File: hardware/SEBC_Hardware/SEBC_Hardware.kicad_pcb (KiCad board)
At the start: 2 copper layers, 38 parts, among them J1 Barrel_Jack_Switch, J2 Conn_01x01_Female, J3 Conn_01x01_Female, J4 AudioJack2_Ground_Switch, J5 Conn_01x01_Female, J6 Conn_01x01_Female, J7 AudioJack2_Ground_Switch, J8 Micro_SD_Card, SW1 SW_Push, SW2 SW_Push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

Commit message: :construction: SEBC PCB
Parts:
- moved C7 210.7 mm to (53.3, 53.3)
- moved C2 208.3 mm to (61.5, 59.9)
- moved R8 202.2 mm to (63.5, 40.6), turned to 270 degrees
- moved D4 195.3 mm to (76.7, 81.3)
- moved C1 191.8 mm to (61.5, 53.3)
- moved C4 186.1 mm to (77.7, 37.1)
- moved SW2 173.8 mm to (91.7, 29.3), turned to 90 degrees
- moved R3 158.6 mm to (86.9, 36.6), turned to 90 degrees
- moved SW1 150.2 mm to (96.8, 36.3), turned to 270 degrees
- moved R4 129.2 mm to (107.3, 36.8), turned to 90 degrees
- moved D3 103.2 mm to (77.7, 30.0)
- moved R7 94.8 mm to (63.5, 72.6), turned to 90 degrees
- moved D2 88.8 mm to (102.1, 36.6), turned to 90 degrees
- moved D1 42.7 mm to (85.3, 84.3)
- moved J1 37.5 mm to (99.1, 82.3)
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
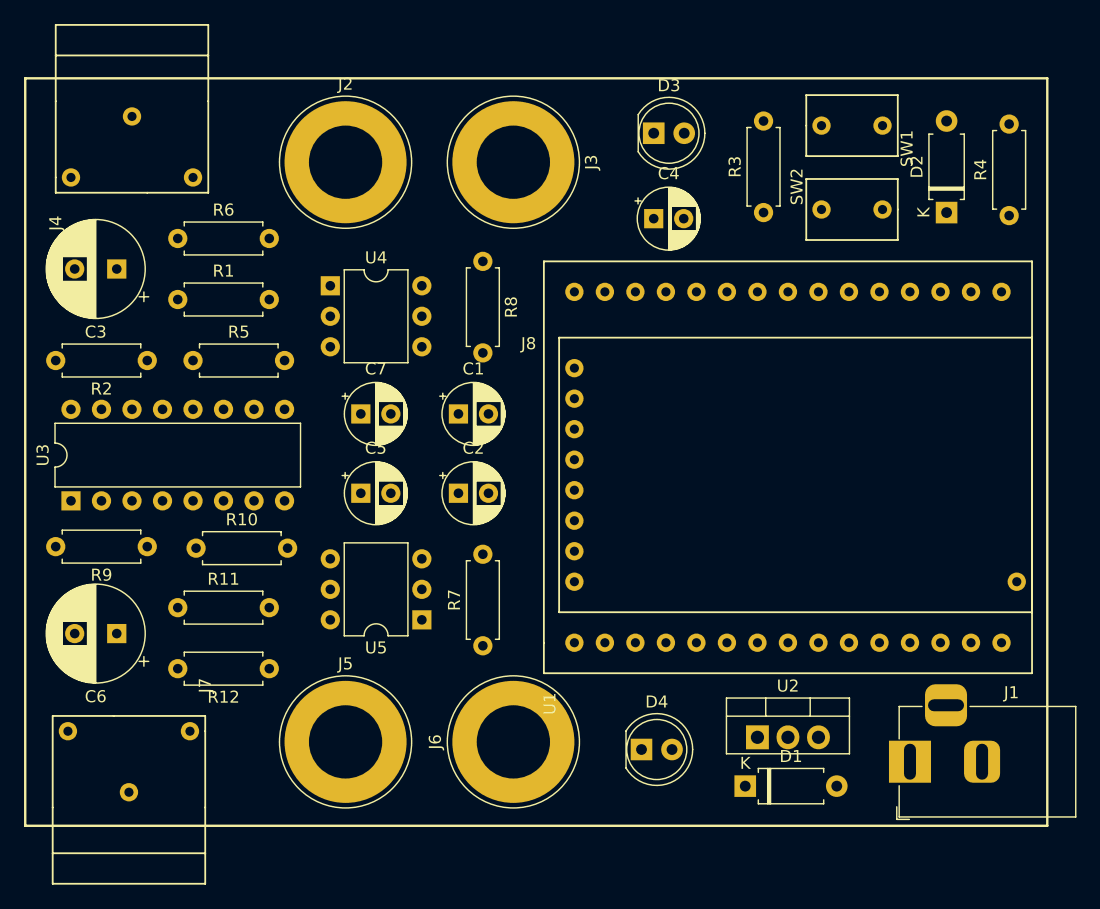
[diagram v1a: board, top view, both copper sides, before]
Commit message: :zap: ADD `PCB
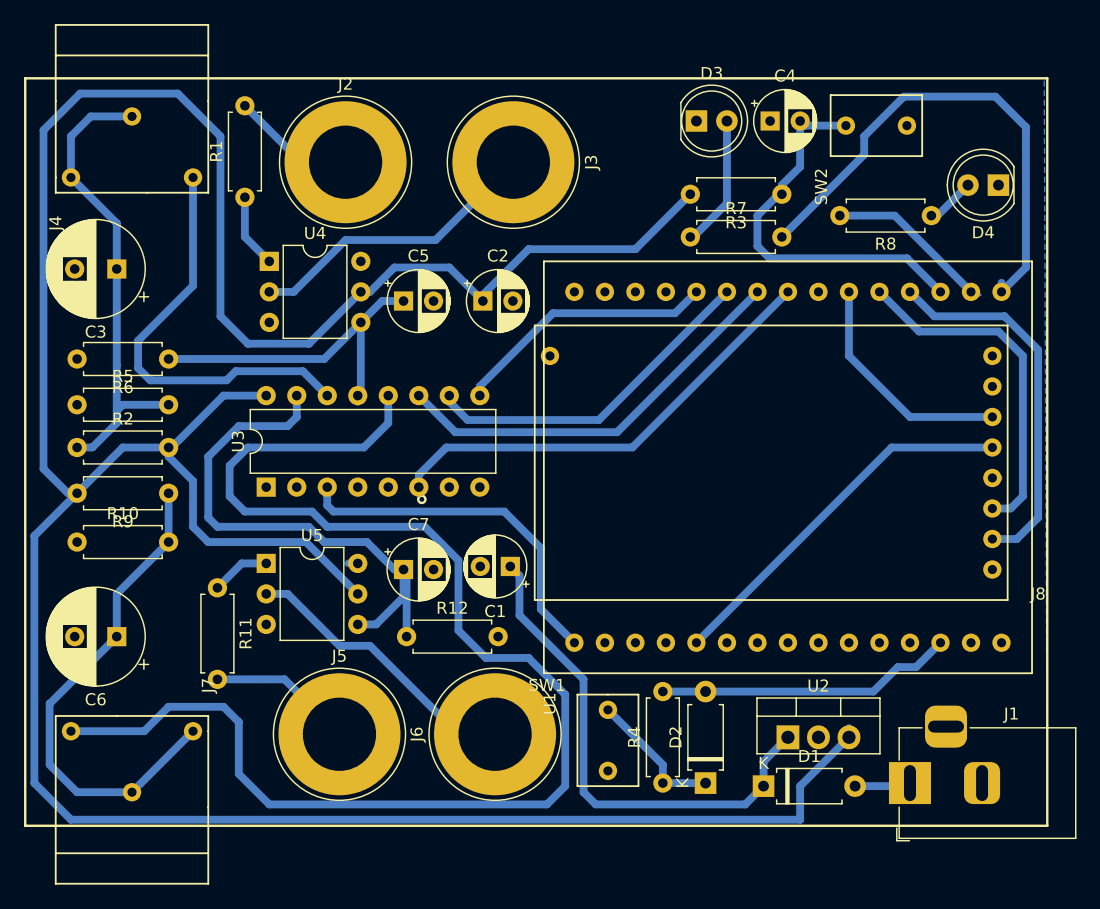
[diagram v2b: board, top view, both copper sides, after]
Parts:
- moved D4 55.6 mm to (106.4, 34.3), turned to 180 degrees
- moved R4 55.3 mm to (78.5, 84.1)
- moved D2 51.6 mm to (82.0, 84.1)
- moved SW1 47.5 mm to (73.9, 78.0), turned to 0 degrees
- moved J8 38.6 mm to (105.9, 66.3), turned to 180 degrees
- moved R7 38.2 mm to (80.8, 38.6), turned to 0 degrees
- moved R8 37.5 mm to (100.8, 36.8), turned to 180 degrees
- moved C5 16.4 mm to (56.9, 43.9)
- moved U3 16.3 mm to (45.5, 59.4)
- moved C2 16.1 mm to (63.5, 43.9)
- moved U5 13.8 mm to (45.5, 65.8), turned to 0 degrees
- moved C7 13.4 mm to (56.9, 66.3)
- moved C1 13.4 mm to (65.8, 66.0), turned to 180 degrees
- moved C4 12.6 mm to (87.4, 29.0)
- moved R12 11.7 mm to (57.1, 71.9), turned to 0 degrees
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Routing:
- net +5V: track 0.00 -> 255.4 mm
- net /SENSOR_C_B: track 0.00 -> 113.8 mm
- net /SENSOR_T_B: track 0.00 -> 46.9 mm
- net /LED_01: track 0.00 -> 42.4 mm
- net Net-(C1-Pad1): track 0.00 -> 42.3 mm
- net Net-(C6-Pad1): track 0.00 -> 41.7 mm
- net Net-(C3-Pad1): track 0.00 -> 40.4 mm
- net /INN_E: track 0.00 -> 38.1 mm, vias 0 -> 1
- net /SENSOR_C_A: track 0.00 -> 35.1 mm
- net /A0: track 0.00 -> 34.3 mm
- net /Boot: track 0.00 -> 33.1 mm
- net /SD4: track 0.00 -> 31.4 mm
- net /SD1: track 0.00 -> 31.2 mm
- net /S_MUX: track 0.00 -> 30.1 mm
- net /SD2: track 0.00 -> 28.8 mm
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- added copper zone on B.Cu, net GND

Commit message: :zap: Improving PCB performance
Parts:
- moved D4 3.64 mm to (105.7, 30.7), turned to 270 degrees
- moved J6 3.05 mm to (61.5, 80.0)
- moved J5 2.30 mm to (49.3, 79.8)
- moved R12 2.05 mm to (59.2, 71.6)
- moved C1 2.05 mm to (63.8, 66.3), turned to 0 degrees
- moved R8 1.85 mm to (100.3, 35.1)
- moved C2 1.08 mm to (64.3, 43.2), turned to 90 degrees
- moved R5 0.76 mm to (29.7, 51.8)
- moved R6 0.76 mm to (37.3, 48.0)
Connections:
- U1 pad 4: /SD3 -> /SD4
- U1 pad 5: /SD4 -> /SD3
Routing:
- net /SD3: track 0.51 -> 33.1 mm
- net /LED_01: track 42.4 -> 27.0 mm
- net +5V: track 255.4 -> 263.8 mm
- net /SENSOR_C_B: track 113.8 -> 107.2 mm
- net /SD4: track 31.4 -> 36.7 mm
- net Net-(C6-Pad1): track 41.7 -> 46.2 mm
- net Net-(J5-Pad1): track 14.3 -> 11.9 mm
- net Net-(D4-Pad2): track 4.10 -> 6.07 mm
- net /SD2: track 28.8 -> 27.4 mm
- net /LED_02: track 14.7 -> 15.9 mm
- net GND: track 0.00 -> 1.08 mm
- net Net-(C1-Pad1): track 42.3 -> 43.0 mm
- net /SD1: track 31.2 -> 30.6 mm
- net /INN_E: vias 1 -> 0
